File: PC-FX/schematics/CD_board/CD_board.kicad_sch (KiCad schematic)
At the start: 69 parts, among them CN101 Conn_01x18_Socket, CN102 Conn_01x10_Pin, CN103 Conn_01x07_Pin, CN104 Conn_01x06_Pin, CN105 Conn_01x03_Socket, IC101 CXA1610M, IC106 BA4510F, IC108 BA4510F, IC118 74AHC1G04, Q101 PNP

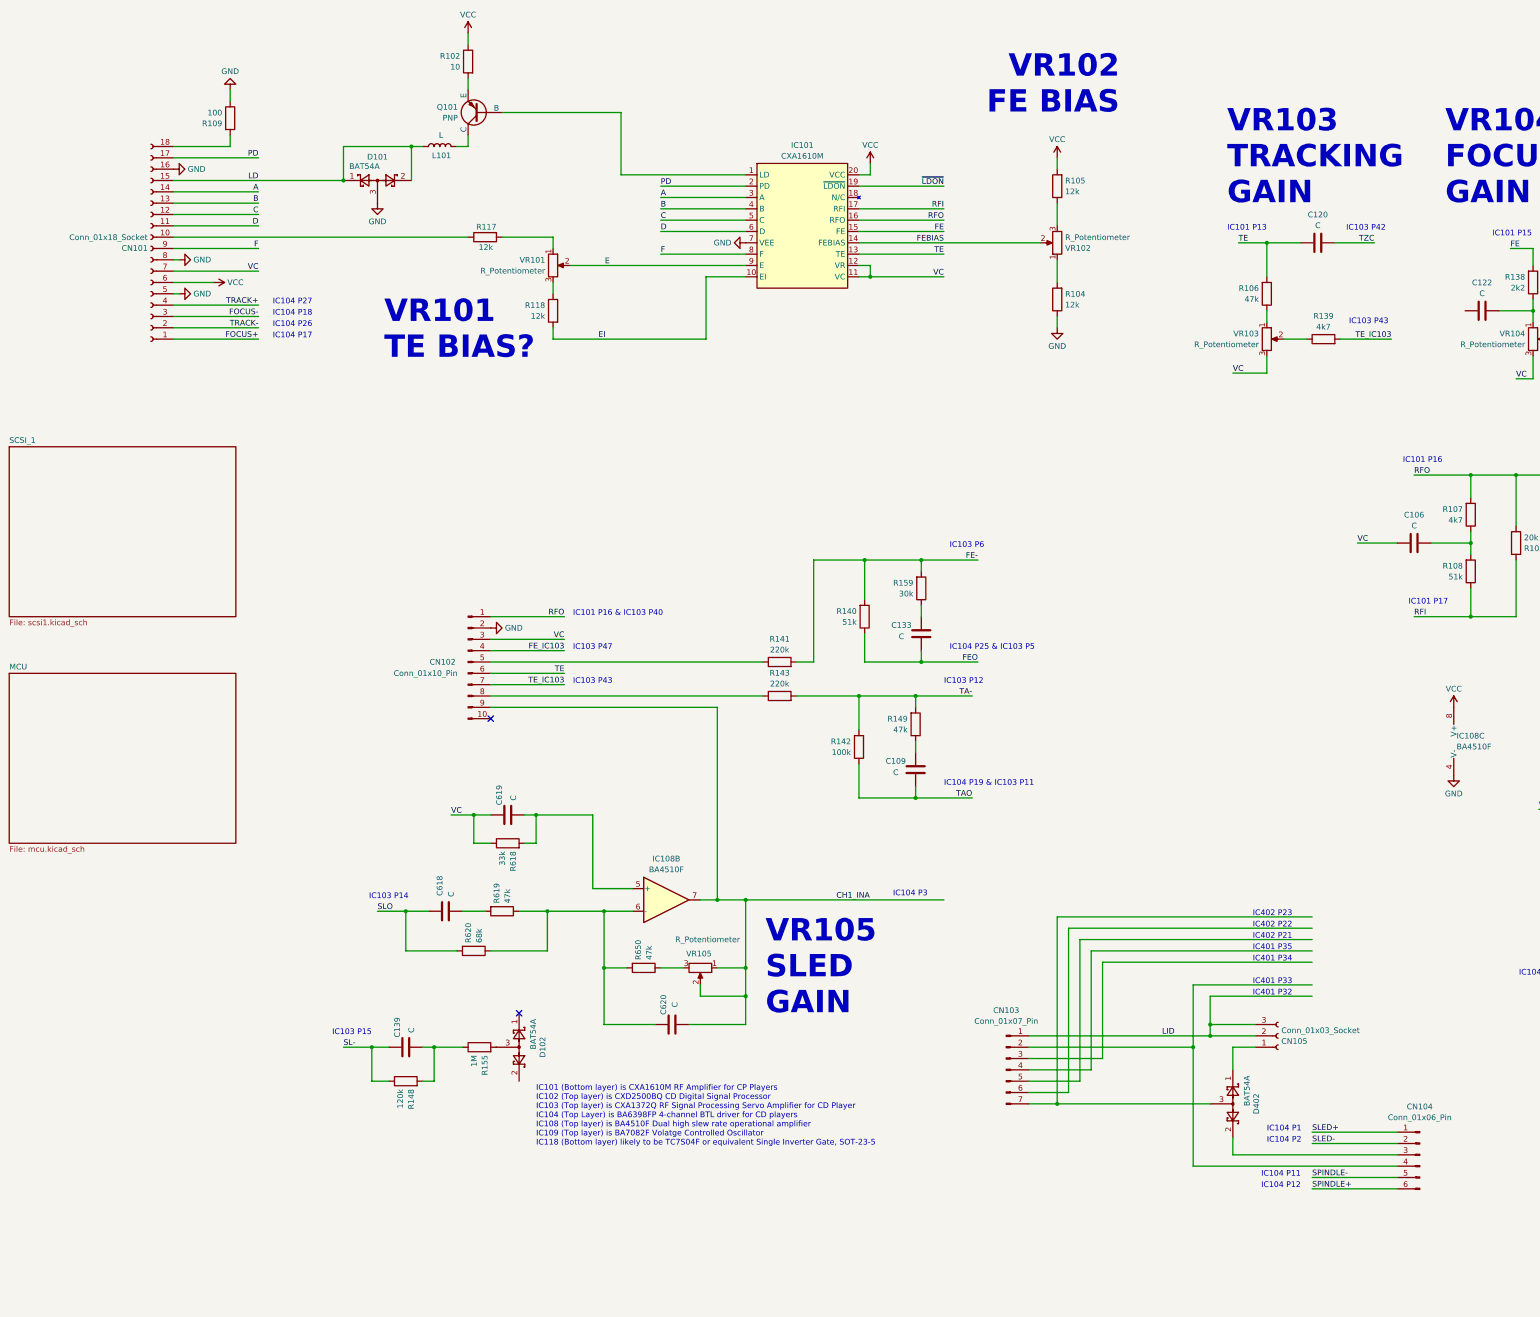
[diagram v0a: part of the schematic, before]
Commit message: PCM sheet complete
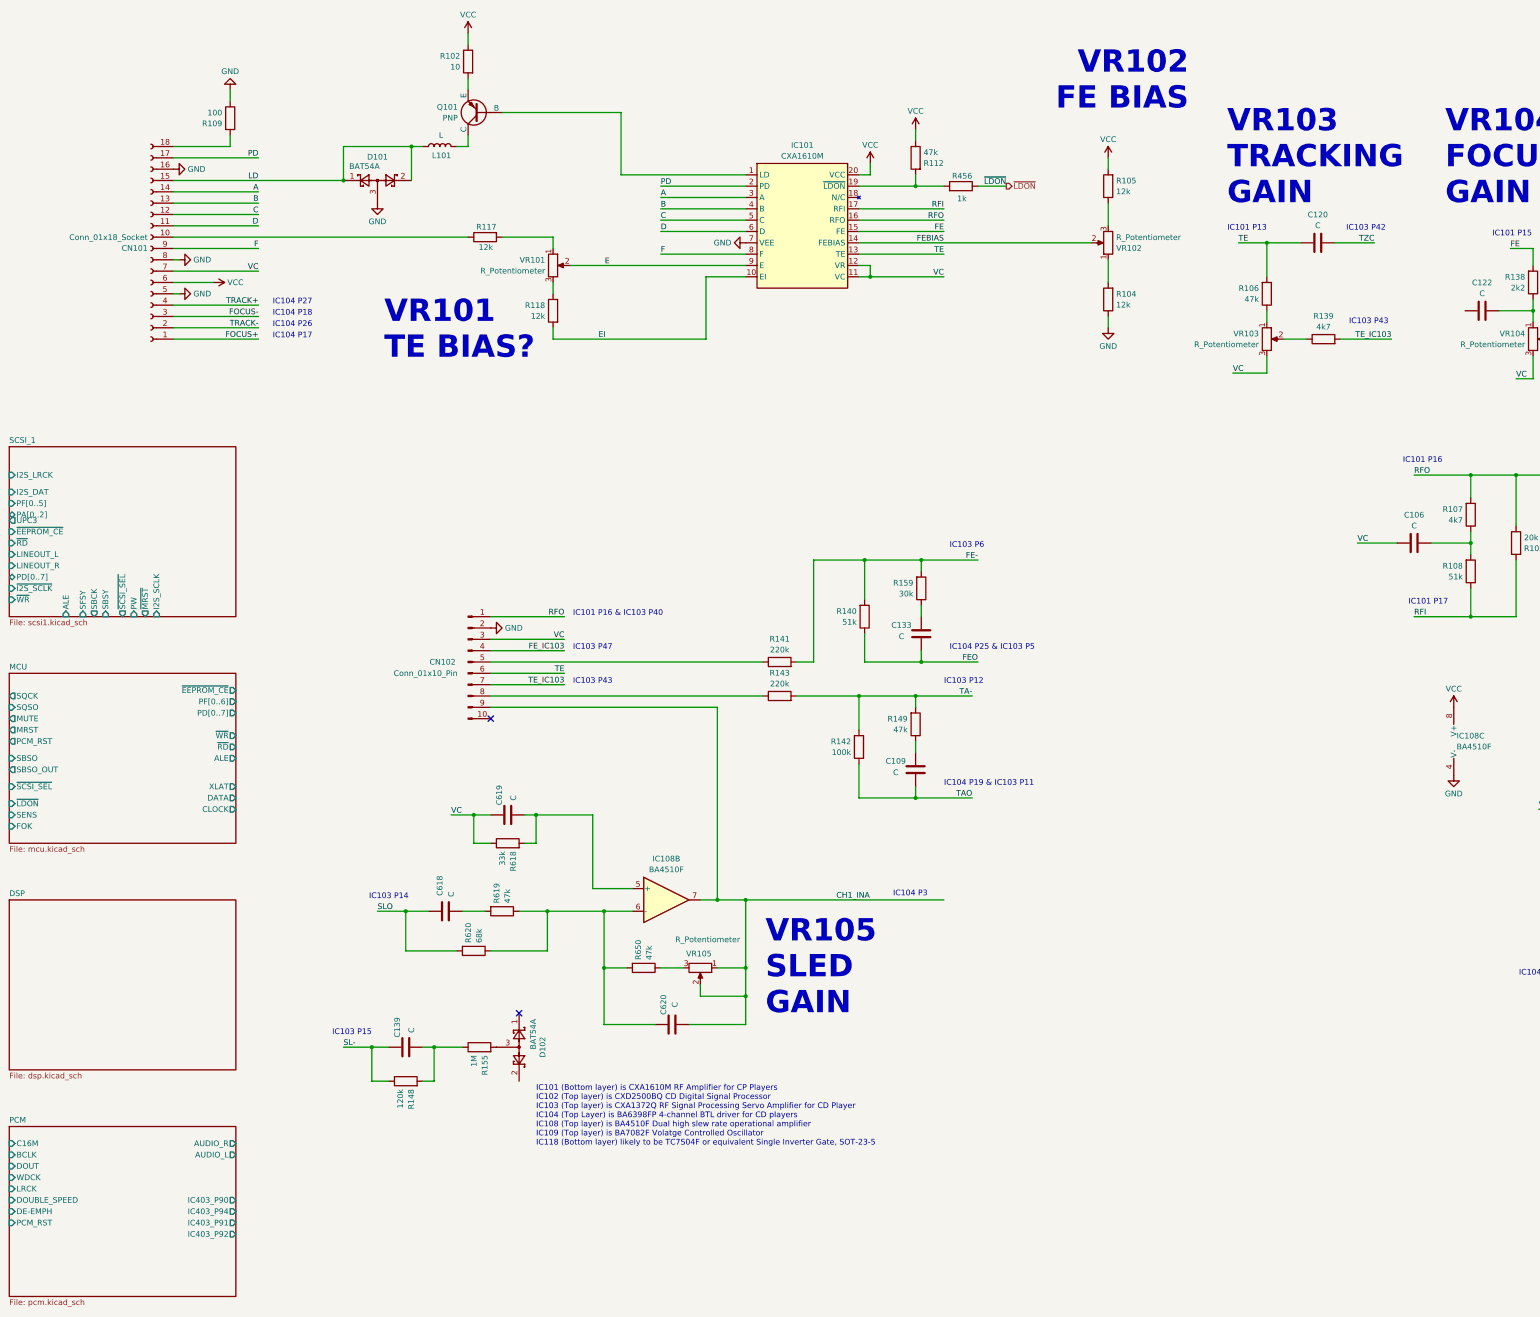
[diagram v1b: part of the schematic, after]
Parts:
- removed CN103: Conn_01x07_Pin, symbol Connector:Conn_01x07_Pin
- removed CN104: Conn_01x06_Pin, symbol Connector:Conn_01x06_Pin
- removed CN105: Conn_01x03_Socket, symbol Connector:Conn_01x03_Socket
- removed D402: BAT54A, Package_TO_SOT_SMD:SOT-23, symbol Diode:BAT54A
- added R112: 47k, symbol Device:R
- added R456: 1k, symbol Device:R
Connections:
- net VCC: now also R112.1
- net ~{LDON}: now also R456.1; no longer IC101.19 (~{LDON})
- new net: IC101.19 (~{LDON}), R112.2, R456.2
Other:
- added sheet DSP (dsp.kicad_sch)
- added sheet PCM (pcm.kicad_sch)
- sheet MCU ports: added ALE, CLOCK, DATA, FOK, MRST, MUTE, PCM_RST, PD[0..7], PF[0..6], SBSO, SBSO_OUT, SENS, SQCK, SQSO, XLAT, ~{EEPROM_CE}, ~{LDON}, ~{RD}, ~{SCSI_SEL}, ~{WR}; removed none
- sheet SCSI_1 ports: added ALE, I2S_DAT, I2S_LRCK, I2S_SCLK, LINEOUT_L, LINEOUT_R, PA[0..2], PD[0..7], PF[0..5], PW, SBCK, SBSY, SFSY, UPC3, ~{EEPROM_CE}, ~{I2S_SCLK}, ~{MRST}, ~{RD}, ~{SCSI_SEL}, ~{WR}; removed none
- note removed: "IC104 P1"
- note removed: "IC104 P11"
- note removed: "IC104 P12"
- note removed: "IC104 P2"
- note removed: "IC401 P32"
- note removed: "IC401 P33"
- note removed: "IC401 P34"
- note removed: "IC401 P35"
- note removed: "IC402 P21"
- note removed: "IC402 P22"
- note removed: "IC402 P23"
- moved on the sheet: R104, R105, VR102

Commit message: Progress mainly on SCSI chips and connections to the MCU
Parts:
- removed IC106: BA4510F, Package_SO:SSOP-8_5.25x5.24mm_P1.27mm, symbol PC-FX:BA4510F
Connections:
- net IC106_P7: now reaches CN102.10 (Pin_10)
- no-connect marks 2 -> 1
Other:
- sheet MCU ports: added CN401_P24, IC401_PB0, IC401_PB1, IC402_P21, IC402_P22, IC402_P23, IC402_P93, IC402_P95, IC402_P96, IC403_P69, PF[0..7], SCOR; removed PF[0..6], ~{EEPROM_CE}
- sheet SCSI_1 ports: added BCLK, CN401_P17, CN401_P18, CN401_P19, CN401_P20, CN401_P23, CN401_P26, CN401_P27, CN401_P8, DOUBLE_SPEED, DOUT, IC402_P21, IC402_P22, IC402_P23, IC402_P93, IC402_P95, IC402_P96, IC403_P69, LRCK, PF[0..7], SCOR, SCSI_D[0..7], WDCK, XTAO; removed I2S_DAT, I2S_LRCK, I2S_SCLK, LINEOUT_L, LINEOUT_R, PA[0..2], PF[0..5], PW, SBCK, SBSY, SFSY, UPC3, ~{EEPROM_CE}, ~{I2S_SCLK}, ~{SCSI_SEL}
- note removed: "IC104 P10"
- note removed: "IC104 P3 & P4"

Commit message: Update on DSP sheet mainly.
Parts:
- removed C157: C, symbol Device:C
- removed CN101: Conn_01x18_Socket, symbol Connector:Conn_01x18_Socket
- removed D101: BAT54A, Package_TO_SOT_SMD:SOT-23, symbol Diode:BAT54A
- removed IC101: CXA1610M, Package_SO:SOIC-20W_7.5x12.8mm_P1.27mm, symbol PC-FX:CXA1610M
- removed IC118: 74AHC1G04, symbol 74xGxx:74AHC1G04
- removed L101: L, symbol Device:L
- removed Q101: PNP, symbol Simulation_SPICE:PNP
- removed R102: 10, symbol Device:R
- removed R104, R105, R117, R118: 12k, symbol Device:R
- removed R109: 100, symbol Device:R
- removed R112: 47k, symbol Device:R
- removed R167, R168, R169: ?, symbol Device:R
- removed R172: 33k, symbol Device:R
- removed R456: 1k, symbol Device:R
- removed TP101, TP140: TestPoint, symbol Connector:TestPoint
- removed VR101, VR102, VR106: R_Potentiometer, Potentiometer_THT:Potentiometer_Bourns_3339P_Vertical, symbol Device:R_Potentiometer
- added CN401: Conn_01x40, symbol Connector_Generic:Conn_01x40
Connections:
- net VCC is gone; now on net GND: IC108.8 (V+)
- net GND: now also CN401.1 (Pin_1), CN401.10 (Pin_10), CN401.16 (Pin_16), CN401.22 (Pin_22), CN401.29 (Pin_29), CN401.3 (Pin_3), CN401.35 (Pin_35), CN401.40 (Pin_40), CN401.5 (Pin_5), CN401.7 (Pin_7)
- new net: CN401.15 (Pin_15), CN401.21 (Pin_21), CN401.28 (Pin_28), CN401.34 (Pin_34), CN401.6 (Pin_6), CN401.9 (Pin_9)
- new net AUDIO_L: CN401.2 (Pin_2)
- new net AUDIO_R: CN401.4 (Pin_4)
- new net CN401_P17: CN401.17 (Pin_17)
- new net CN401_P18: CN401.18 (Pin_18)
- new net CN401_P19: CN401.19 (Pin_19)
- new net CN401_P20: CN401.20 (Pin_20)
- new net CN401_P23: CN401.23 (Pin_23)
- new net CN401_P24: CN401.24 (Pin_24)
- new net CN401_P26: CN401.26 (Pin_26)
- new net CN401_P27: CN401.27 (Pin_27)
- new net CN401_P8: CN401.8 (Pin_8)
- new net EXCK: CN401.14 (Pin_14)
- new net SBSO: CN401.13 (Pin_13)
- new net SCOR: CN401.12 (Pin_12)
- new net SCSI_D0: CN401.39 (Pin_39)
- new net SCSI_D1: CN401.38 (Pin_38)
- new net SCSI_D2: CN401.37 (Pin_37)
- new net SCSI_D3: CN401.36 (Pin_36)
- new net SCSI_D4: CN401.33 (Pin_33)
- new net SCSI_D5: CN401.32 (Pin_32)
- new net SCSI_D6: CN401.31 (Pin_31)
- new net SCSI_D7: CN401.30 (Pin_30)
- new net WFCK: CN401.11 (Pin_11)
- new net ~{EXRST}: CN401.25 (Pin_25)
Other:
- sheet SCSI_1 renamed SCSI
- added sheet RF Amplifer (rfamp.kicad_sch)
- sheet DSP ports: added C16M, CLOCK, DATA, DE-EMPH, DOUBLE_SPEED, DSP_BCLK, DSP_DOUT, DSP_LRCK, DSP_WDCK, EXCK, FOK, FSW, IC106_P7, IC401_PB0, IC401_PB1, LOCK, MDP, MDS, MON, MRST, MUTE, PDO, SBSO, SCOR, SENS, SPO, SQCK, SQSO, VCOI, VCOO, WFCK, XLAT, XTAO, ~{LDON}; removed none
- sheet MCU ports: added ~{EXRST}, ~{INRST_EN}; removed IC403_P69, SBSO, SBSO_OUT, ~{SCSI_SEL}
- sheet PCM ports: added DSP_BCLK, DSP_DOUT, DSP_LRCK, DSP_WDCK; removed IC403_P90, IC403_P91, IC403_P92, IC403_P94
- sheet SCSI ports: added ~{INRST_EN}; removed IC403_P69
- note added: "IC101 (Bottom layer) is CXA1610M RF Amplifier for CP Players IC102 (Top layer) is CXD2500BQ CD Digital Signal Processor IC103 (Top layer) is CXA1372Q RF Signal Processing Servo Amplifier for CD Player IC104 (Top Layer) is BA6398FP 4-channel BTL driver for CD players IC108 (Top layer) is BA4510F Dual high slew rate operational amplifier IC109 (Top layer) is BA7082F Voltage Controlled Oscillator IC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"
- note added: "Is SCSI_~{BSY} bidirectional? That would require another connection. Last connection could be Is SCSI_~{ATN}"
- note added: "SCSI_~{ACK} ?"
- note added: "SCSI_~{BSY} ?"
- note added: "SCSI_~{CD} ?"
- note added: "SCSI_~{IO} ?"
- note added: "SCSI_~{MSG} ?"
- note added: "SCSI_~{REQ} ?"
- note added: "SCSI_~{SEL} ?"
- note removed: "IC101 (Bottom layer) is CXA1610M RF Amplifier for CP Players IC102 (Top layer) is CXD2500BQ CD Digital Signal Processor IC103 (Top layer) is CXA1372Q RF Signal Processing Servo Amplifier for CD Player IC104 (Top Layer) is BA6398FP 4-channel BTL driver for CD players IC108 (Top layer) is BA4510F Dual high slew rate operational amplifier IC109 (Top layer) is BA7082F Volatge Controlled Oscillator IC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"
- note removed: "IC102 P13 (VCTL)"
- note removed: "IC102 P14 (VO)"
- note removed: "IC102 P17 (VCKI)"
- note removed: "IC104 P17"
- note removed: "IC104 P18"
- note removed: "IC104 P26"
- note removed: "IC104 P27"
- note removed: "IC109 P7 (FO)"
- note removed: "IC109 P9"
- note removed: "VR101 TE BIAS?"
- note removed: "VR102 FE BIAS"
- note removed: "VR106 FADJ"

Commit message: Schematics pretty much done. Expect some mistakes but it captures enough information to help understanding its behaviour.
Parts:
- removed C106, C109, C119, C120, C122, C133, C139, C614, C617, C618, C619, C620: C, symbol Device:C
- removed CN102: Conn_01x10_Pin, symbol Connector:Conn_01x10_Pin
- removed D102, D601: BAT54A, Package_TO_SOT_SMD:SOT-23, symbol Diode:BAT54A
- removed IC108: BA4510F, Package_SO:SSOP-8_5.25x5.24mm_P1.27mm, symbol PC-FX:BA4510F
- removed R103: 20k, symbol Device:R
- removed R106, R149, R619, R650: 47k, symbol Device:R
- removed R107, R139: 4k7, symbol Device:R
- removed R108, R140: 51k, symbol Device:R
- removed R138: 2k2, symbol Device:R
- removed R141, R143: 220k, symbol Device:R
- removed R142, R610, R616: 100k, symbol Device:R
- removed R148: 120k, symbol Device:R
- removed R155: 1M, symbol Device:R
- removed R159: 30k, symbol Device:R
- removed R613, R620: 68k, symbol Device:R
- removed R614: 22k, symbol Device:R
- removed R615: 1k, symbol Device:R
- removed R618: 33k, symbol Device:R
- removed VR103, VR104, VR105: R_Potentiometer, Potentiometer_THT:Potentiometer_Bourns_3339P_Vertical, symbol Device:R_Potentiometer
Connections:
- net VCC: now reaches CN401.15 (Pin_15), CN401.21 (Pin_21), CN401.28 (Pin_28), CN401.34 (Pin_34), CN401.6 (Pin_6), CN401.9 (Pin_9)
- no-connect marks 1 -> 0
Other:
- added sheet POWER (power.kicad_sch)
- added sheet SERVO (servo.kicad_sch)
- sheet DSP ports: added ASY, C.OUT, CLKO, DATO, EFM, MIRR, SERVO_SENS, XLTO, ~{MRST}, ~{SERVO_RST}; removed DOUBLE_SPEED, FSW, IC106_P7, IC401_PB0, IC401_PB1, MDS, MON, MRST, PDO, SPO, VCOI, VCOO
- sheet MCU ports: added ENDSW_A, ENDSW_B, IC401_PB4, ~{MRST}; removed MRST
- sheet RF Amplifer ports: added FE, FOCUS+, FOCUS-, RFO, TE, TRACK+, TRACK-, VC, ~{LDON}; removed none
- note removed: "IC101 (Bottom layer) is CXA1610M RF Amplifier for CP Players IC102 (Top layer) is CXD2500BQ CD Digital Signal Processor IC103 (Top layer) is CXA1372Q RF Signal Processing Servo Amplifier for CD Player IC104 (Top Layer) is BA6398FP 4-channel BTL driver for CD players IC108 (Top layer) is BA4510F Dual high slew rate operational amplifier IC109 (Top layer) is BA7082F Voltage Controlled Oscillator IC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"
- note removed: "IC101 P13"
- note removed: "IC101 P15"
- note removed: "IC101 P16"
- note removed: "IC101 P16 & IC103 P40"
- note removed: "IC101 P17"
- note removed: "IC103 P12"
- note removed: "IC103 P14"
- note removed: "IC103 P15"
- note removed: "IC103 P18"
- note removed: "IC103 P33 & IC102 P1"
- note removed: "IC103 P39"
- note removed: "IC103 P40"
- note removed: "IC103 P42"
- note removed: "IC103 P43"
- note removed: "IC103 P47"
- note removed: "IC103 P6"
- note removed: "IC104 P19 & IC103 P11"
- note removed: "IC104 P25 & IC103 P5"
- note removed: "IC104 P3"
- note removed: "Positive Gain x4"
- note removed: "VR103 TRACKING GAIN"
- note removed: "VR104 FOCUS GAIN"
- note removed: "VR105 SLED GAIN"
- title: PC FX Pots Adfustment Schematics -> PC-FX CD Board Schematics
- moved on the sheet: CN401

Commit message: Small update based on confirmation of SCSI control signals
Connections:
- net CN401_P17 renamed SCSI_~{IO}
- net CN401_P18 renamed SCSI_~{REQ}
- net CN401_P19 renamed SCSI_~{CD}
- net CN401_P20 renamed SCSI_~{MSG}
- net CN401_P23 renamed SCSI_~{BSY}
- net CN401_P24 renamed SCSI_~{SEL}
- net CN401_P26 renamed SCSI_~{ACK}
- net CN401_P27 renamed SCSI_~{ATN}
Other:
- sheet MCU ports: added SCSI_~{SEL}, SWITCH_STROBE; removed CN401_P24, IC402_P23
- sheet SCSI ports: added SCSI_~{ACK}, SCSI_~{ATN}, SCSI_~{BSY}, SCSI_~{CD}, SCSI_~{IO}, SCSI_~{MSG}, SCSI_~{REQ}, SWITCH_STROBE; removed CN401_P17, CN401_P18, CN401_P19, CN401_P20, CN401_P23, CN401_P26, CN401_P27, IC402_P23
- note added: "CN401 comments: To comply with SCSI specs, SCSI_~{BSY} and SCSI_~{SEL} should be bidirectional. But is it the case? All pins are pull low through a 4.7k resistor except P8 which is neither pulled up/down. P8 is constanly low and it seems to be like a CD board ready or present pin."
- note removed: "Is SCSI_~{BSY} bidirectional? That would require another connection. Last connection could be Is SCSI_~{ATN}"
- note removed: "SCSI_~{ACK} ?"
- note removed: "SCSI_~{BSY} ?"
- note removed: "SCSI_~{CD} ?"
- note removed: "SCSI_~{IO} ?"
- note removed: "SCSI_~{MSG} ?"
- note removed: "SCSI_~{REQ} ?"
- note removed: "SCSI_~{SEL} ?"
